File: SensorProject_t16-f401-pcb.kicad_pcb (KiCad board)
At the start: 2 copper layers, 48.3 x 71.1 mm, 56 parts, among them J1 Conn_01x02_Pin, J10 Conn_01x02_Pin, J11 Conn_01x02_Pin, J12 Conn_01x02_Pin, J13 Conn_01x02_Pin, J14 Conn_01x02_Pin, J15 Conn_01x02_Pin, J16 Conn_01x02_Pin, J17 Conn_01x04_Pin, J18 PinSocket_1x20_P2.54mm_Vertic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, J19 PinSocket_1x20_P2.54mm_Vertic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, J2 Conn_01x02_Pin, J20 Screw_Terminal_01x02, J3 Conn_01x02_Pin, J4 Conn_01x02_Pin, J5 Conn_01x02_Pin, J6 Conn_01x02_Pin, J7 Conn_01x02_Pin, J8 Conn_01x02_Pin, J9 Conn_01x02_Pin, U1 ADS1115IDGS, U2 ADS1115IDGS, U3 ADS1115IDGS, U4 ADS1115IDGS

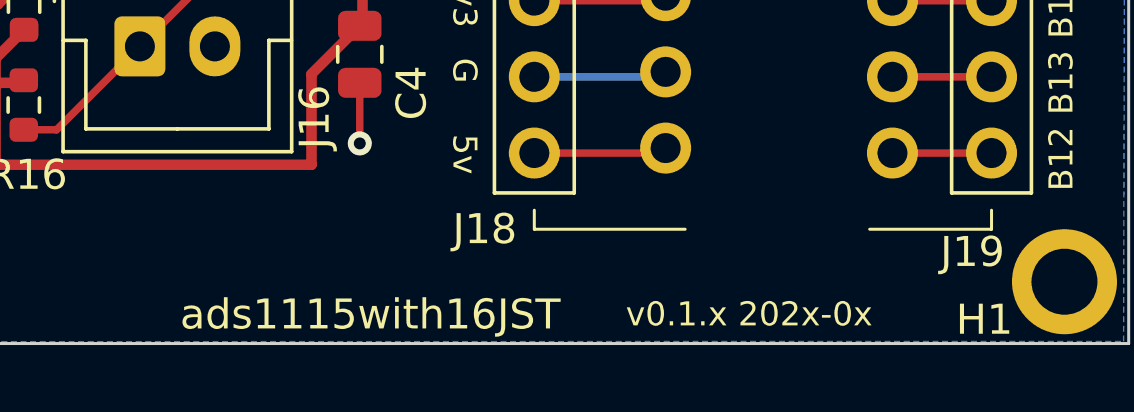
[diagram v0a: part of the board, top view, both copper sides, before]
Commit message: mv/rename ads1115with16JTS to SensorProject_t16-f401-pcb
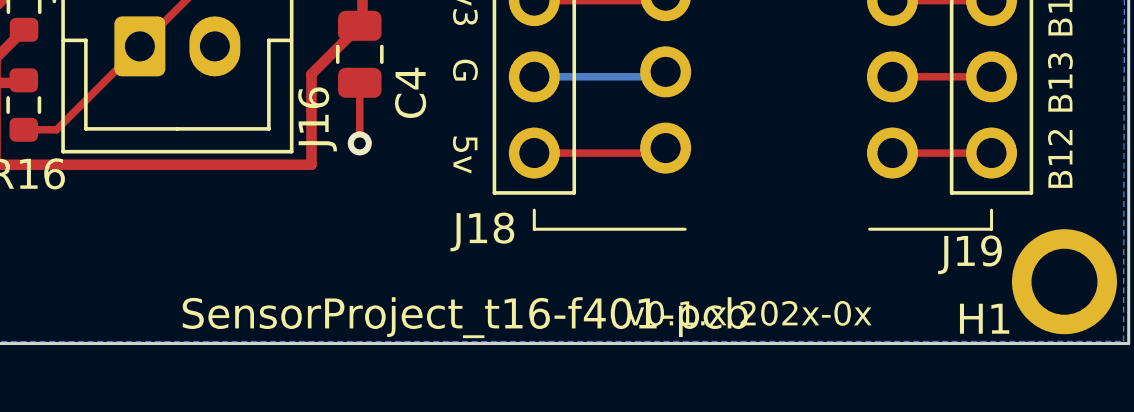
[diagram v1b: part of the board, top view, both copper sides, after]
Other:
- board text added: "SensorProject_t16-f401-pcb"
- board text removed: "ads1115with16JST"

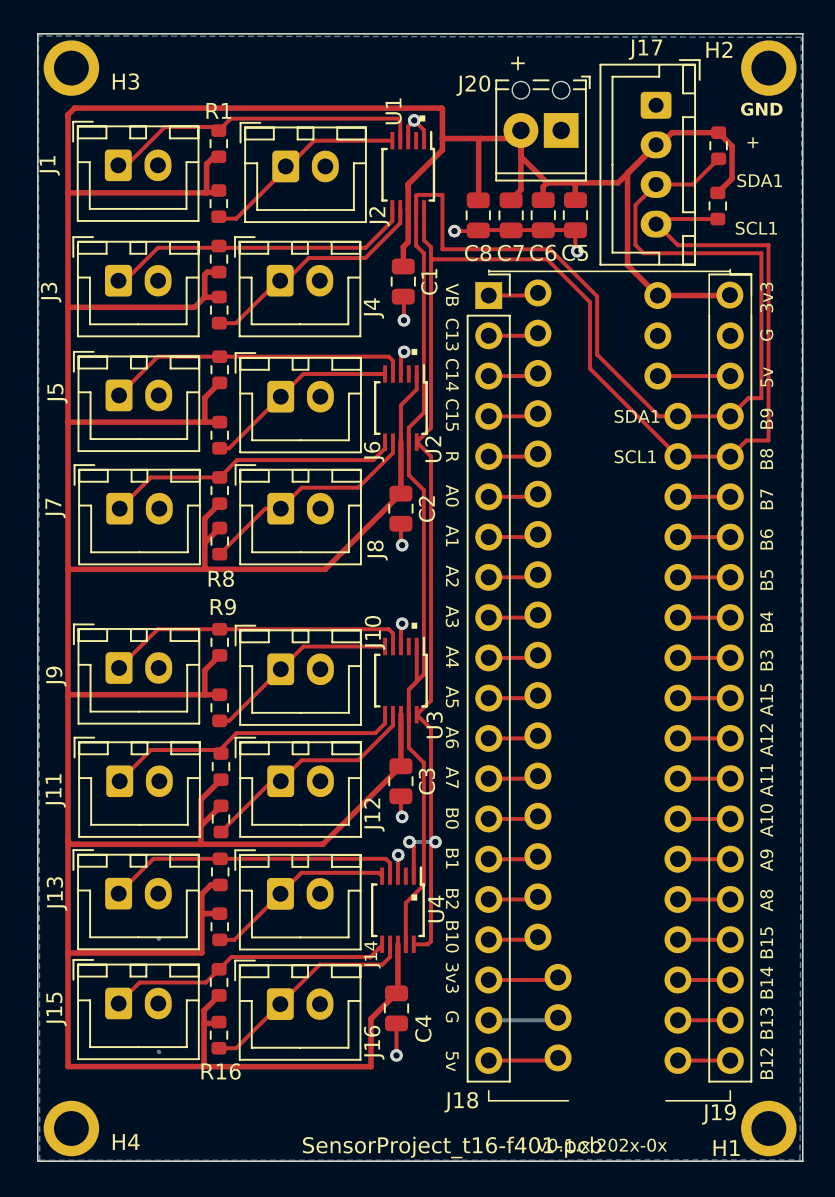
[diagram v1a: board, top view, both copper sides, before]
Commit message: added 10k pullups on ads alert/rdy pins.
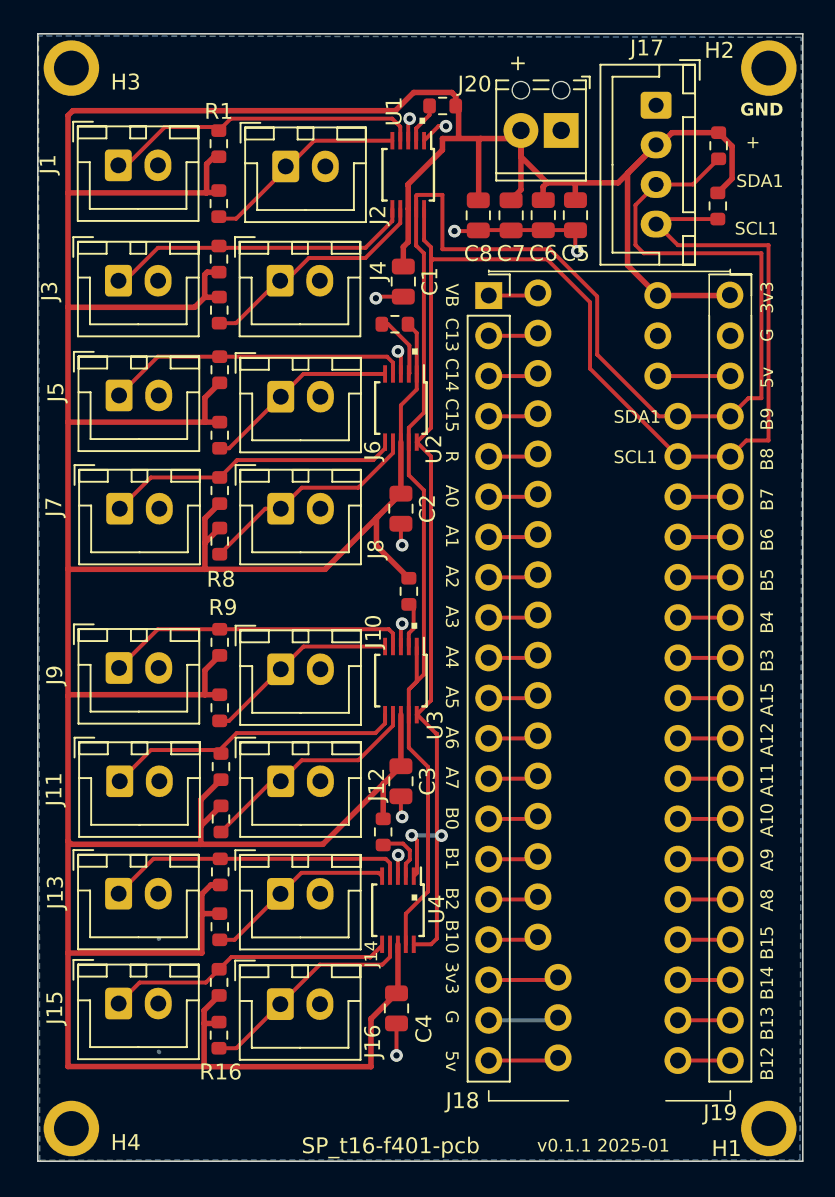
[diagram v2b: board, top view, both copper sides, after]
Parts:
- added R19: 10k, ProjectLib:R_0603_1608Metric, F.Cu at (75.1, 28.7)
- added R20: 10k, ProjectLib:R_0603_1608Metric, F.Cu at (72.1, 42.5)
- added R21: 10k, ProjectLib:R_0603_1608Metric, F.Cu at (72.9, 59.3)
- added R22: 10k, ProjectLib:R_0603_1608Metric, F.Cu at (71.3, 74.5)
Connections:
- U1 pad 2: unconnected-(U1-ALERT/RDY-Pad2) -> Net-(U1-ALERT/RDY)
- U2 pad 2: unconnected-(U2-ALERT/RDY-Pad2) -> Net-(U2-ALERT/RDY)
- U3 pad 2: unconnected-(U3-ALERT/RDY-Pad2) -> Net-(U3-ALERT/RDY)
- U4 pad 2: unconnected-(U4-ALERT/RDY-Pad2) -> Net-(U4-ALERT/RDY)
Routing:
- net +3V3: track 314.3 -> 325.3 mm
- net Net-(U2-ALERT/RDY): track 0.00 -> 4.11 mm
- net Net-(U4-ALERT/RDY): track 0.00 -> 3.50 mm
- net Net-(U3-ALERT/RDY): track 0.00 -> 2.91 mm
- net Net-(U1-ALERT/RDY): track 0.00 -> 2.54 mm
- net Net-(J4-Pin_1): track 15.9 -> 14.4 mm
- net /SCL1: track 105.8 -> 106.6 mm
- net Net-(J12-Pin_1): track 14.3 -> 13.8 mm
- net Net-(J1-Pin_1): track 20.0 -> 19.5 mm
- net GND: track 27.2 -> 27.5 mm, vias 10 -> 11
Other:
- board text added: "SP_t16-f401-pcb"
- board text added: "v0.1.1 2025-01"
- board text removed: "SensorProject_t16-f401-pcb"
- board text removed: "v0.1.x 202x-0x"
